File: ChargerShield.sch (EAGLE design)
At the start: 28 parts, among them IC1 LM358N, Q1 BD648, Q2 BD648, T2 BC548, X1 +5V, X2 Battery, X3 VCC

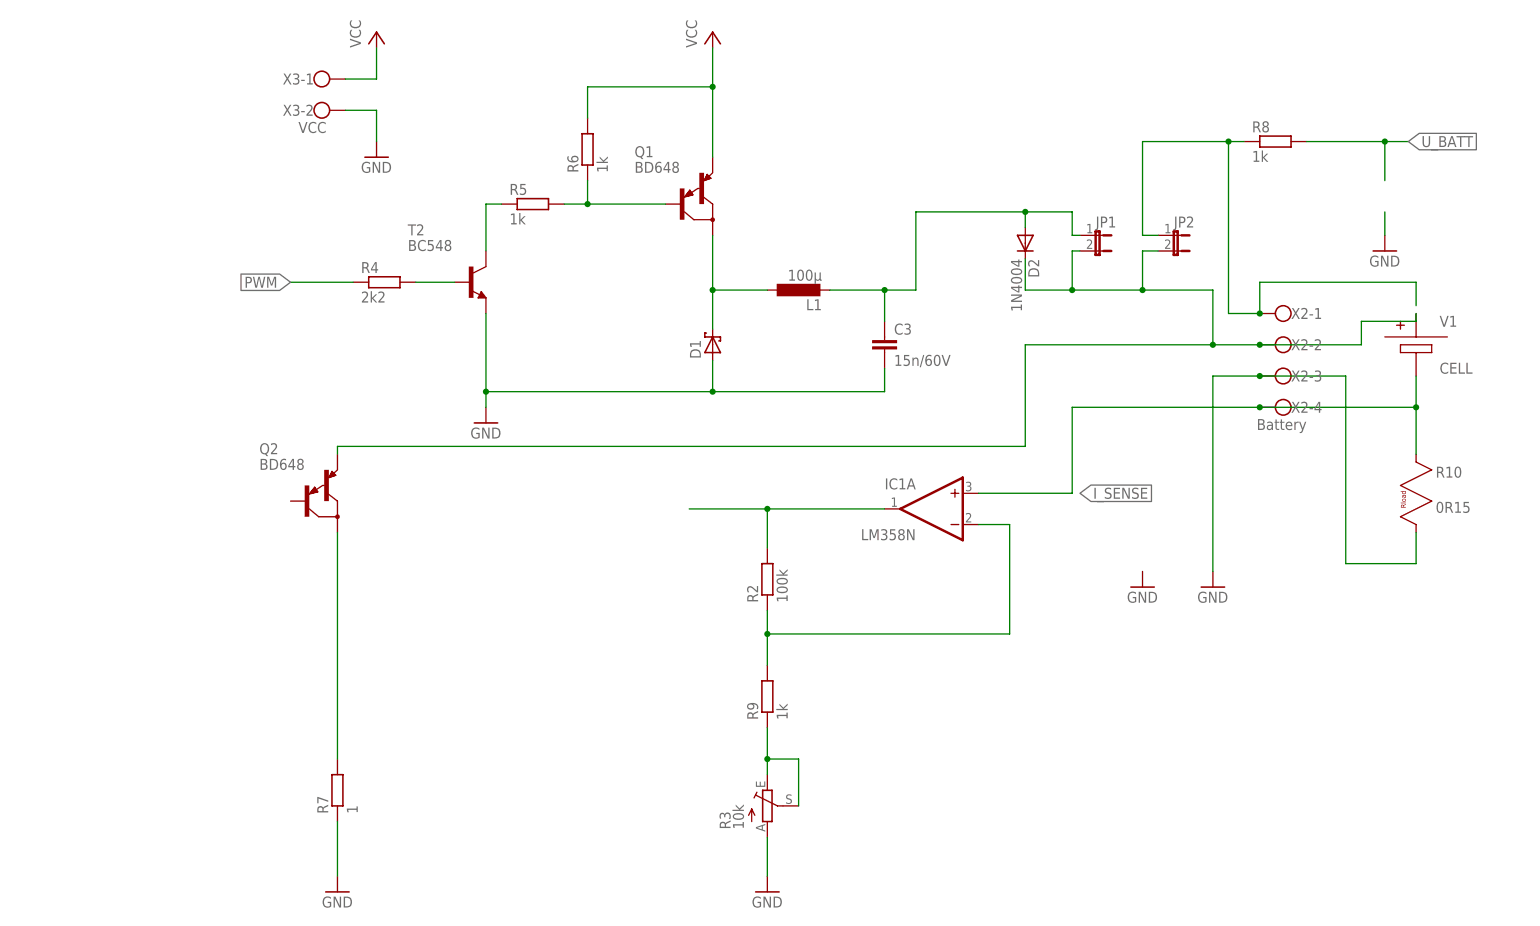
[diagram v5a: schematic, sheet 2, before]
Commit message: longer Arduino shield
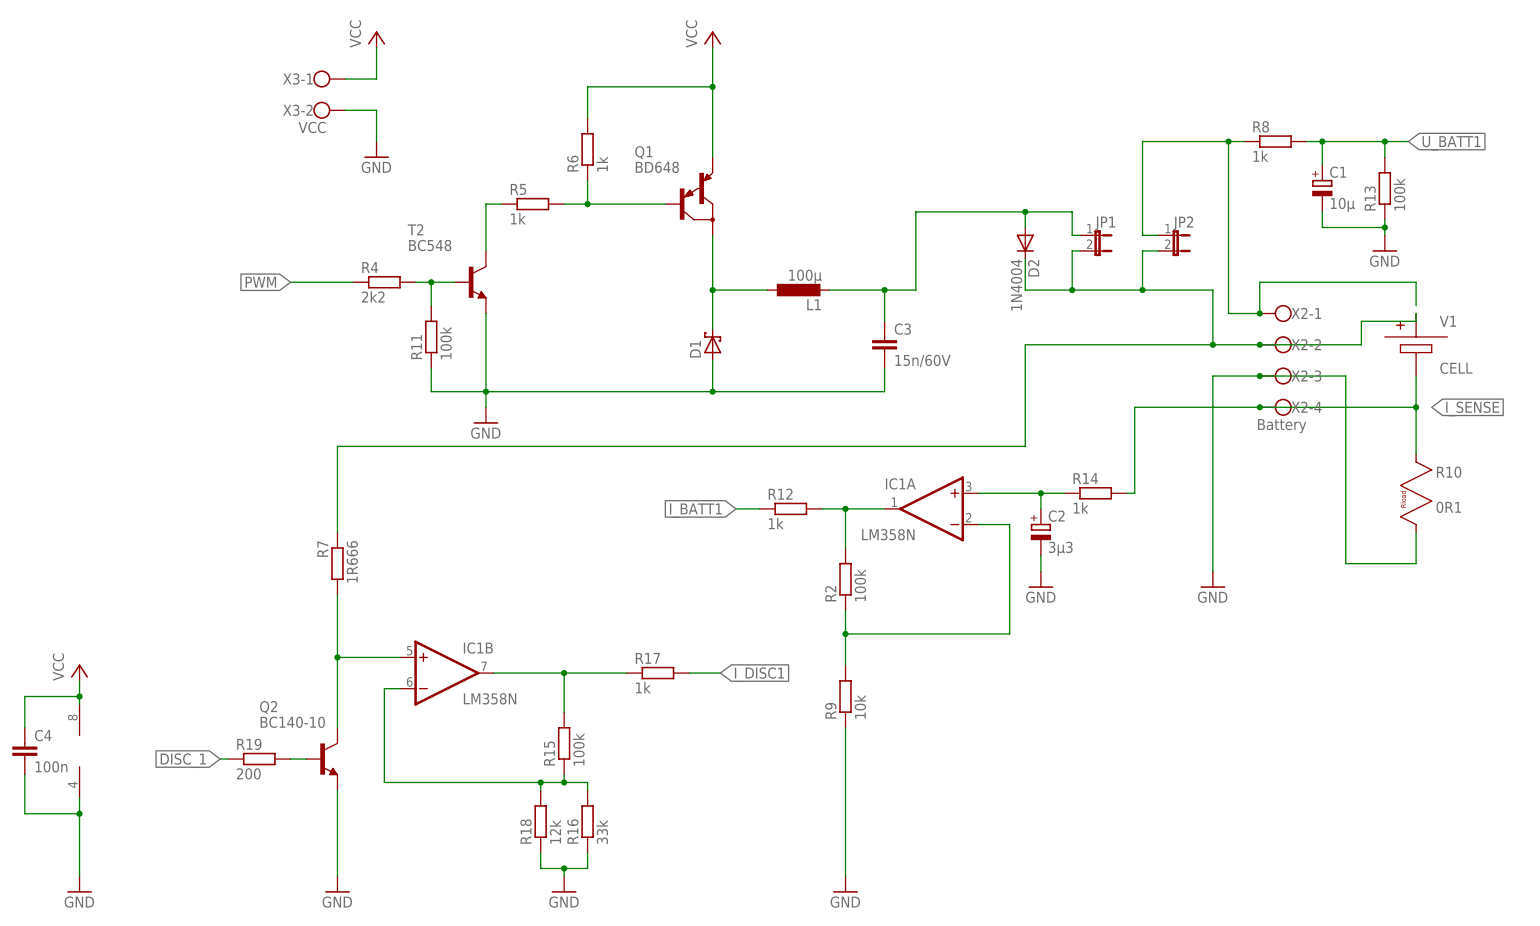
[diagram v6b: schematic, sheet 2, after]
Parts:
- removed R3: 10k, pot:TRIM_EU-LI10
- added C1: 10µ, rcl:CPOL-EUE5-5
- added C2: 3µ3, rcl:CPOL-EUE5-5
- added C4: 100n, rcl:C-EU025_050-025X075
- added LED2: (no value), bigger:LED5MM_BIG
- added Q3: BC548, transistor-npn:BC548
- added R11, R15: 100k, rcl:R-EU_0207/10
- added R12: 1k, rcl:R-EU_0207/10
- added R13: 100k, rcl:R-EU_0207/12
- added R14: 1k, rcl:R-EU_0204/5
- added R16: 33k, rcl:R-EU_0207/10
- added R17, R20: 1k, rcl:R-EU_0207/15
- added R18: 12k, rcl:R-EU_0207/10
- added R19: 200, rcl:R-EU_0207/10
- added S3: Start, SparkFun-Electromechanical:SWITCH-MOMENTARY-2PTH
- added S4: Discharge, SparkFun-Electromechanical:SWITCH-MOMENTARY-2PTH
- Q2: value BD648 -> BC140-10; device transistor-pnp:BD648 -> transistor-npn:BC140-10
- R10: value 0R15 -> 0R1
- R2: device rcl:R-EU_0207/10 -> rcl:R-EU_0204/7
- R5: device rcl:R-EU_0207/15 -> rcl:R-EU_0207/10
- R7: value 1 -> 1R666
- R8: device rcl:R-EU_0207/10 -> rcl:R-EU_0207/15
- R9: value 1k -> 10k; device rcl:R-EU_0207/10 -> rcl:R-EU_0207/12
- S2: value UP -> Up
- U$1: value ARDUINOUNO -> ARDUINOR3BPLACE-LONG; device adafruit:ARDUINOUNO -> arduino-long:ARDUINOR3BPLACE-LONG
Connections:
- removed net U_BATT: R8.2, U$1.A0
- new net DISC_1: Q3.E, R19.1
- new net I_BATT1: R12.1, U$1.A1
- new net I_DISC1: R17.2, U$1.A2
- new net N$16: IC1B.-IN, R15.1, R16.2, R18.2
- new net N$17: IC1B.OUT, R15.2, R17.1
- new net N$18: Q2.B, R19.2
- new net N$20: Q3.B, R20.2
- new net N$21: LED2.C, Q3.C
- new net N$22: S3.2, U$1.D8
- new net N$23: S4.2, U$1.D12
- new net N$24: R20.1, U$1.D10
- new net U_BATT1: C1.+, R13.2, R8.2, U$1.A0
- net +5V: now also LED2.A
- net GND: now also C1.-, C2.-, C4.2, IC1P.V-, Q2.E, R11.1, R13.1, R16.1, R18.1, R9.1, S3.1, S4.1, U$1.GND1, U$1.GND2; no longer R3.A, R7.1
- net I_SENSE: now also R14.2; no longer IC1A.+IN
- net N$11: now also R12.2
- net N$12: now also IC1B.+IN
- net N$13: now also R7.1; no longer Q2.E
- net N$15: now also C2.+, IC1A.+IN, R14.1; no longer R3.E, R3.S, R9.1
- net N$3: now also U$1.D4; no longer U$1.D3
- net N$4: now also U$1.D7; no longer U$1.D4
- net N$5: now also R11.2
- net VCC: now also C4.1, IC1P.V+
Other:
- moved on the sheet: LED1, R1, R2, R7, R9, S2

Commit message: LM324
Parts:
- IC1: value LM358N -> LM324N; device linear:LM358N -> linear:LM324N
- R14: device rcl:R-EU_0204/5 -> rcl:R-EU_0207/10
- R8: device rcl:R-EU_0207/15 -> rcl:R-EU_0207/10
- R9: device rcl:R-EU_0207/12 -> rcl:R-EU_0207/10
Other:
- note added: "what the fuck? muesste oben am R sein!"
- moved on the sheet: R15, R16, R17, R18

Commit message: changes to reflect current breadboard layout
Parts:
- added LED3: CHRG2, bigger:LED5MM_BIG
- added R3: (no value), rcl:R-EU_0207/10
- LED1: value (none) -> CHRG1
- R20: device rcl:R-EU_0207/15 -> rcl:R-EU_0204/7
- R4: device rcl:R-EU_0207/10 -> rcl:R-EU_0207/12
- R5: device rcl:R-EU_0207/10 -> rcl:R-EU_0207/15
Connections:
- net N$24 renamed PWM_DISCHARGE1
- removed net PWM: R4.1, U$1.D9
- new net I_BATT2: U$1.A4/SDA
- new net I_DISC2: U$1.A5/SCL
- new net N$19: R3.2, U$1.D5
- new net N$24: LED3.A, R3.1
- new net PWM_CHARGE1: R4.1, U$1.D3
- new net PWM_CHARGE2: U$1.D9
- new net PWM_DISCHARGE2: U$1.D11
- new net U_BATT2: U$1.A3
- net GND: now also LED3.C
